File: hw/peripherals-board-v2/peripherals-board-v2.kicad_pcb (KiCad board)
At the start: 2 copper layers, 75 x 55 mm, 33 parts, among them J1 Power/Motor Screw Terminal, J10 Extra Servo, J11 Conn_02x05_Odd_Even, J2 OLED, J3 BNO055, J4 LiDAR Right, J5 LiDAR Left, J6 Radio Input, J7 LiDAR Front, J8 Motor Encoder, J9 Steering Servo, SW1 Power, U1 RP2040-Zero, U4 AMS1117-5.0

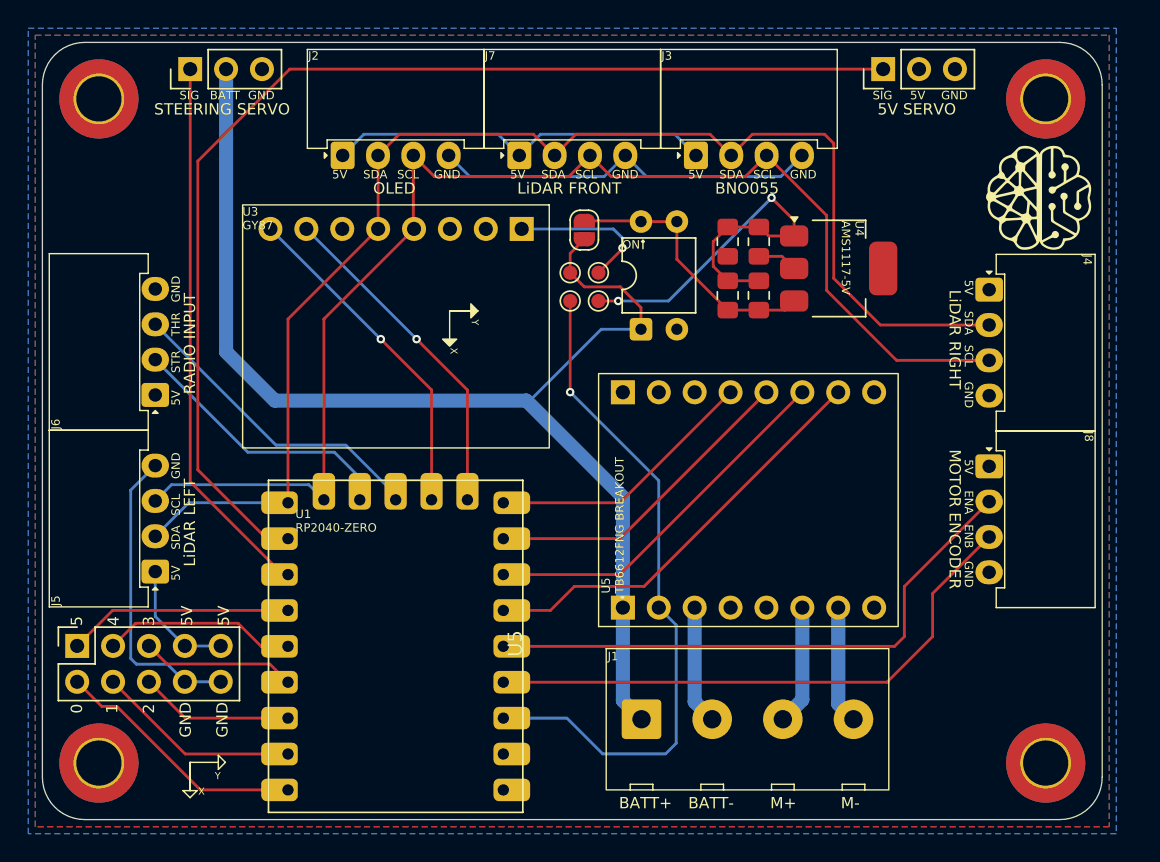
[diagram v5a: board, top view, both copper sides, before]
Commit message: Swap left LiDAR and radio input connectors
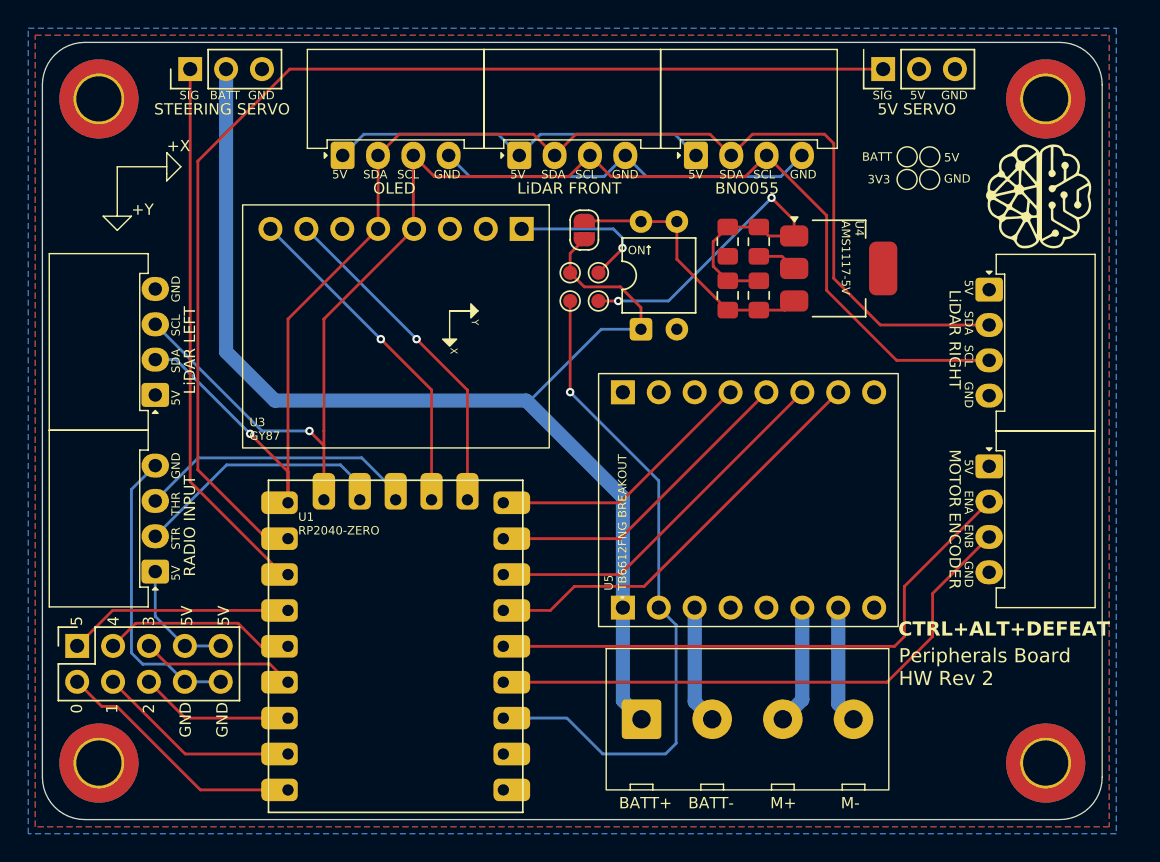
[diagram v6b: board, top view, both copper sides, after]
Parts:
- J5: value LiDAR Left -> Radio Input
- J6: value Radio Input -> LiDAR Left
- moved G*** 0.10 mm to (109.5, 57.9)
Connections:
- J5 pad 2: /I2C0_SDA -> /RX_STR
- J5 pad 3: /I2C0_SCL -> /RX_THR
- J6 pad 2: /RX_STR -> /I2C0_SDA
- J6 pad 3: /RX_THR -> /I2C0_SCL
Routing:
- net /I2C0_SDA: track 95.1 -> 99.6 mm, vias 0 -> 1
- net /I2C0_SCL: track 92.2 -> 94.9 mm, vias 0 -> 1
- net /RX_THR: track 22.4 -> 19.8 mm
- net /RX_STR: track 19.5 -> 18.2 mm
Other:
- board text added: "+X"
- board text added: "+Y"
- board text added: "3V3"
- board text added: "Peripherals Board HW Rev 2"
- board text added: "Peripherals Interface Board Hardware Revision 2 Designed by Adbhut Patil diylabsed.github.io/wro-25"
- board text removed: "Designed by Adbhut Patil"
- board text removed: "J1"
- board text removed: "J2"
- board text removed: "J3"
- board text removed: "J4"
- board text removed: "J5"
- board text removed: "J6"
- board text removed: "J7"
- board text removed: "J8"
- board text removed: "Peripherals Interface Board"
- board text removed: "X"
- board text removed: "Y"
- board text removed: "https://diylabsed.github.io/wro-25"

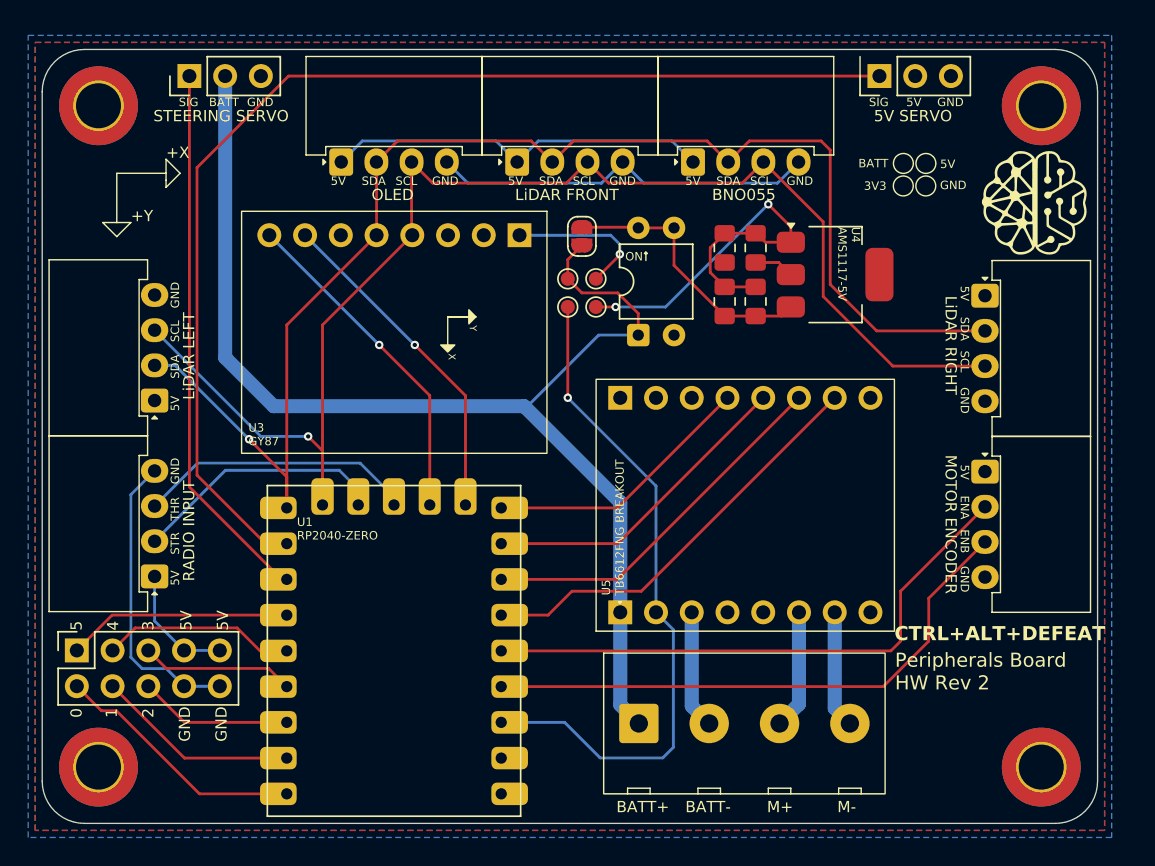
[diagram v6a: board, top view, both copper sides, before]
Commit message: Create footprint and symbol for BNO055 breakout, prototype new layout
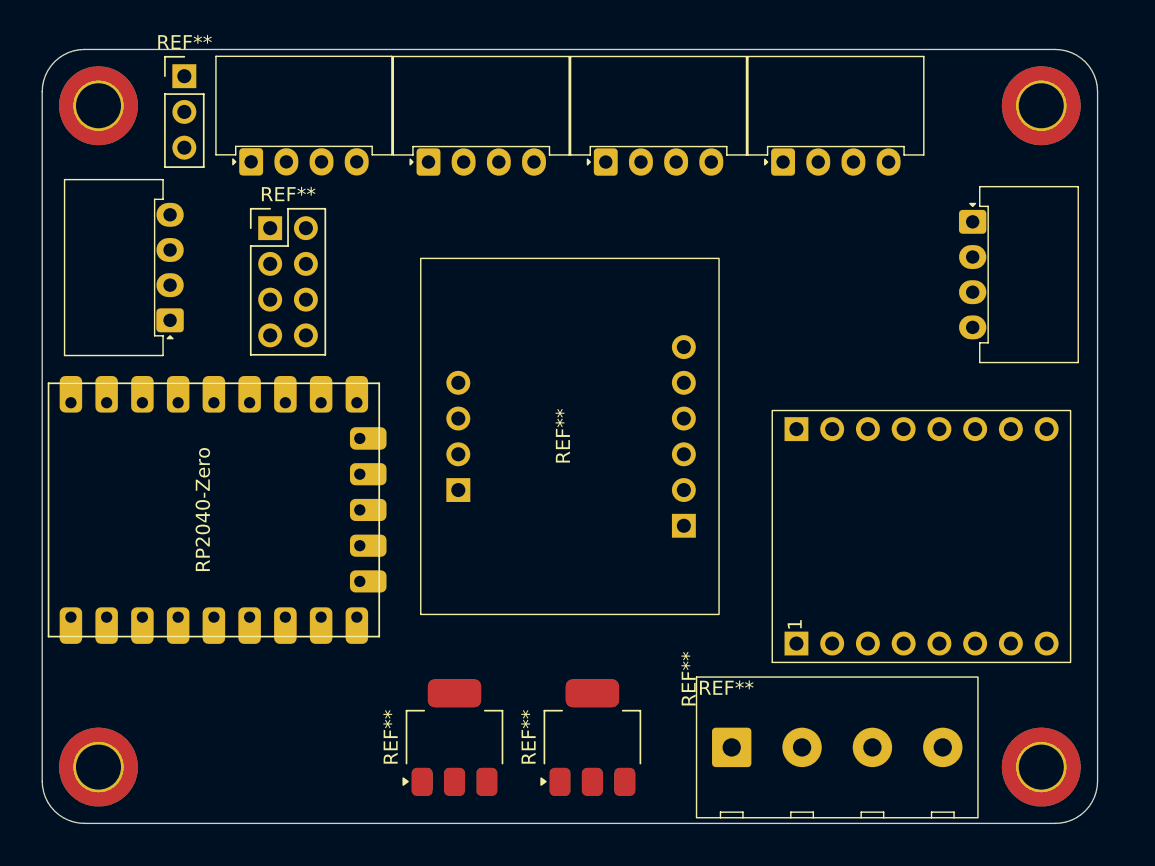
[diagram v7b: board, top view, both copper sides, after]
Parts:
- removed C1, C2: 0.1 uF, Capacitor_SMD:C_0805_2012Metric_Pad1.18x1.45mm_HandSolder
- removed C3, C4: 10 uF, Capacitor_SMD:C_0805_2012Metric_Pad1.18x1.45mm_HandSolder
- removed G*** (x4): LOGO, LOGO
- removed J1: Power/Motor Screw Terminal, ScrewTerminal_01x04_P5mm:ScrewTerminal_01x04_P5mm
- removed J10: Extra Servo, Connector_PinHeader_2.54mm:PinHeader_1x03_P2.54mm_Vertical
- removed J11: Conn_02x05_Odd_Even, Connector_PinSocket_2.54mm:PinSocket_2x05_P2.54mm_Vertical
- removed J2: OLED, JST_XH_01x04_Horizontal_NoFlange:JST_XH_01x04_Horizontal_NoFlange
- removed J3: BNO055, JST_XH_01x04_Horizontal_NoFlange:JST_XH_01x04_Horizontal_NoFlange
- removed J4: LiDAR Right, JST_XH_01x04_Horizontal_NoFlange:JST_XH_01x04_Horizontal_NoFlange
- removed J5: Radio Input, JST_XH_01x04_Horizontal_NoFlange:JST_XH_01x04_Horizontal_NoFlange
- removed J6: LiDAR Left, JST_XH_01x04_Horizontal_NoFlange:JST_XH_01x04_Horizontal_NoFlange
- removed J7: LiDAR Front, JST_XH_01x04_Horizontal_NoFlange:JST_XH_01x04_Horizontal_NoFlange
- removed J8: Motor Encoder, JST_XH_01x04_Horizontal_NoFlange:JST_XH_01x04_Horizontal_NoFlange
- removed J9: Steering Servo, Connector_PinHeader_2.54mm:PinHeader_1x03_P2.54mm_Vertical
- removed JP1: SW1 Bypass, Jumper:SolderJumper-2_P1.3mm_Open_RoundedPad1.0x1.5mm
- removed SW1: Power, Package_DIP:DIP-4_W7.62mm
- removed TP1: GND, TestPoint:TestPoint_Pad_D1.0mm
- removed TP2: +5V, TestPoint:TestPoint_Pad_D1.0mm
- removed TP3: +3.3V, TestPoint:TestPoint_Pad_D1.0mm
- removed TP4: +BATT, TestPoint:TestPoint_Pad_D1.0mm
- removed U1: RP2040-Zero, RP2040-Zero:RP2040-Zero
- removed U3: ~, GY87:GY87
- removed U4: AMS1117-5.0, Package_TO_SOT_SMD:SOT-223-3_TabPin2
- removed U5: ~, TB6612FNG-breakout:TB6612FNG-breakout
- added REF**: JST_XH_01x04_Horizontal_NoFlange, JST_XH_01x04_Horizontal_NoFlange:JST_XH_01x04_Horizontal_NoFlange, F.Cu at (105.1, 59.2)
- added REF**: JST_XH_01x04_Horizontal_NoFlange, JST_XH_01x04_Horizontal_NoFlange:JST_XH_01x04_Horizontal_NoFlange, F.Cu at (66.5, 55.0)
- added REF**: RP2040-Zero, RP2040-Zero:RP2040-Zero, F.Cu at (63.9, 89.9)
- added REF**: JST_XH_01x04_Horizontal_NoFlange, JST_XH_01x04_Horizontal_NoFlange:JST_XH_01x04_Horizontal_NoFlange, F.Cu at (53.9, 55.0)
- added REF**: SOT-223, Package_TO_SOT_SMD:SOT-223, F.Cu at (78.1, 95.9)
- added REF**: JST_XH_01x04_Horizontal_NoFlange, JST_XH_01x04_Horizontal_NoFlange:JST_XH_01x04_Horizontal_NoFlange, F.Cu at (79.0, 55.0)
- added REF**: BNO055-breakout, BNO055-breakout:BNO055-breakout, F.Cu at (76.5, 74.5)
- added REF**: JST_XH_01x04_Horizontal_NoFlange, JST_XH_01x04_Horizontal_NoFlange:JST_XH_01x04_Horizontal_NoFlange, F.Cu at (48.1, 66.2)
- added REF**: PinHeader_1x03_P2.54mm_Vertical, Connector_PinHeader_2.54mm:PinHeader_1x03_P2.54mm_Vertical, F.Cu at (49.1, 48.9)
- added REF**: TB6612FNG -breakout, TB6612FNG-breakout:TB6612FNG-breakout, F.Cu at (92.6, 94.3)
- added REF**: SOT-223, Package_TO_SOT_SMD:SOT-223, F.Cu at (68.3, 95.9)
- added REF**: JST_XH_01x04_Horizontal_NoFlange, JST_XH_01x04_Horizontal_NoFlange:JST_XH_01x04_Horizontal_NoFlange, F.Cu at (91.7, 55.0)
- added REF**: PinHeader_2x04_P2.54mm_Vertical, Connector_PinHeader_2.54mm:PinHeader_2x04_P2.54mm_Vertical, F.Cu at (55.2, 59.7)
- added REF**: ScrewTerminal_01x04_P5mm, ScrewTerminal_01x04_P5mm:ScrewTerminal_01x04_P5mm, F.Cu at (92.8, 106.0)
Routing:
- net /I2C0_SDA: track 99.6 -> 0.00 mm, vias 1 -> 0
- net /I2C0_SCL: track 94.9 -> 0.00 mm, vias 1 -> 0
- net +BATT: track 89.2 -> 0.00 mm
- net GND: track 87.5 -> 0.00 mm, vias 2 -> 0
- net /EXT_SERVO: track 81.4 -> 0.00 mm
- net +5V: track 49.6 -> 0.00 mm, vias 1 -> 0
- net +3.3V: track 48.0 -> 0.00 mm, vias 1 -> 0
- net /ENCA: track 40.7 -> 0.00 mm
- net /ENCB: track 40.4 -> 0.00 mm
- net /STR_SERVO: track 38.8 -> 0.00 mm
- net /PWMB: track 30.1 -> 0.00 mm
- net /BIN2: track 26.5 -> 0.00 mm
- net /INT1: track 23.9 -> 0.00 mm, vias 1 -> 0
- net /DRDY: track 23.9 -> 0.00 mm, vias 1 -> 0
- net /BIN1: track 22.9 -> 0.00 mm
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- removed copper zone on B.Cu, net +5V
- removed copper zone on F.Cu, net +5V
- removed copper zone on B.Cu, net GND
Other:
- board text removed: "+X"
- board text removed: "+Y"
- board text removed: "0"
- board text removed: "1"
- board text removed: "2"
- board text removed: "3"
- board text removed: "3V3"
- board text removed: "4"
- board text removed: "5"
- board text removed: "5V"
- board text removed: "5V SERVO"
- board text removed: "BATT"
- board text removed: "BATT+"
- board text removed: "BATT-"
- board text removed: "BNO055"
- board text removed: "CTRL+ALT+DEFEAT"
- board text removed: "ENA"
- board text removed: "ENB"
- board text removed: "GND"
- board text removed: "GitHub Repo"
- board text removed: "LiDAR FRONT"
- board text removed: "LiDAR LEFT"
- board text removed: "LiDAR RIGHT"
- board text removed: "M+"
- board text removed: "M-"
- board text removed: "MOTOR ENCODER"
- board text removed: "OLED"
- board text removed: "ON"
- board text removed: "Peripherals Board HW Rev 2"
- board text removed: "Peripherals Interface Board Hardware Revision 2 Designed by Adbhut Patil diylabsed.github.io/wro-25"
- board text removed: "RADIO INPUT"
- board text removed: "SCL"
- board text removed: "SDA"
- board text removed: "SIG"
- board text removed: "STEERING SERVO"
- board text removed: "STR"
- board text removed: "THR"
- board text removed: "U1 RP2040-ZERO"
- board text removed: "U3 GY87"
- board text removed: "U4 AMS1117-5V"
- board text removed: "U5 TB6612FNG BREAKOUT"
- board text removed: "Website"
